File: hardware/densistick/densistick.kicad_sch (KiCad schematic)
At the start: 58 parts, among them J1 Cable, SW1 SW_Push, U1 TSL2522, U2 USBLC6-2SC6, U3 MIC4812, U4 FT260Q, U5 MIC5365-1.8YC5, U6 CAT24C08, U7 MCP4017-104E/LT

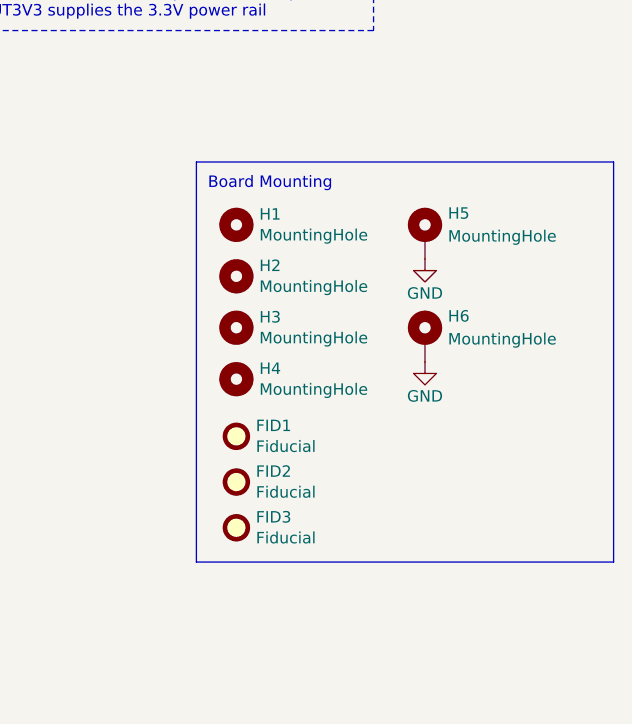
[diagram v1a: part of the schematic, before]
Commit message: Update DensiStick fiducial and position data
Add a fourth fiducial
Adjust some component silkscreen locations for more fiducial clearance
Tweak fiducial locations
Update metadata for position file exclusion
Update board date, but not revision
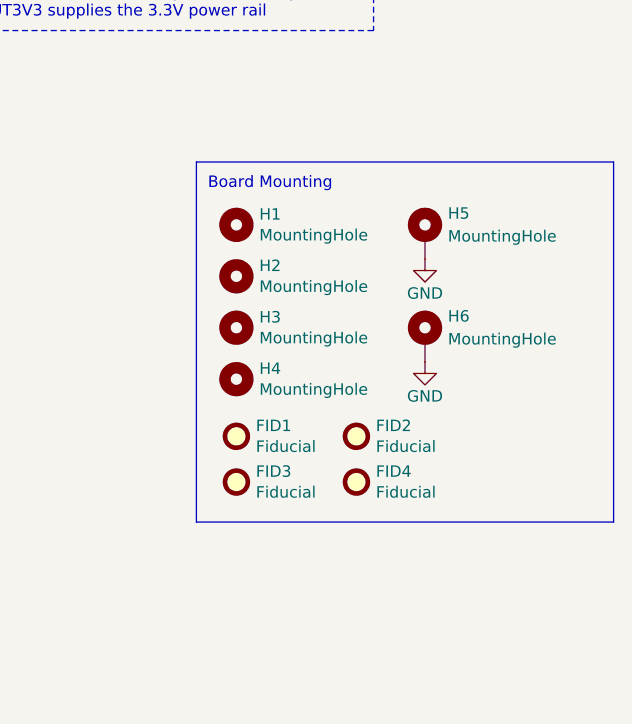
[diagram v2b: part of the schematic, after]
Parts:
- added FID4: Fiducial, Fiducial:Fiducial_1mm_Mask2mm, symbol Mechanical:Fiducial
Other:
- moved on the sheet: FID2, FID3
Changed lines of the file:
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@@
 	(title_block
 		(title "Printalyzer DensiStick")
-		(date "2025-04-30")
+		(date "2026-05-28")
 		(rev "C")
 		(company "Dektronics, Inc.")
@@
 	(rectangle
 		(start 219.075 125.73)
-		(end 265.43 170.18)
+		(end 265.43 165.735)
 		(stroke
 			(width 0)
@@
 		(in_bom no)
 		(on_board yes)
-		(in_pos_files yes)
+		(in_pos_files no)
 		(dnp no)
 		(property "Reference" "H1"
@@
 		(in_bom no)
 		(on_board yes)
-		(in_pos_files yes)
+		(in_pos_files no)
 		(dnp no)
 		(property "Reference" "H2"
@@
 		(in_bom no)
 		(on_board yes)
-		(in_pos_files yes)
+		(in_pos_files no)
 		(dnp no)
 		(property "Reference" "H3"
@@
 		(in_bom no)
 		(on_board yes)
-		(in_pos_files yes)
+		(in_pos_files no)
 		(dnp no)
 		(property "Reference" "H4"
@@
 		(in_bom no)
 		(on_board yes)
-		(in_pos_files yes)
+		(in_pos_files no)
 		(dnp no)
 		(property "Reference" "H5"
@@
 		(in_bom no)
 		(on_board yes)
-		(in_pos_files yes)
+		(in_pos_files no)
 		(dnp no)
 		(property "Reference" "H6"
@@
 	(symbol
 		(lib_id "Mechanical:Fiducial")
-		(at 223.52 161.29 0)
+		(at 236.855 156.21 0)
 		(unit 1)
 		(body_style 1)
@@
 		(dnp no)
 		(property "Reference" "FID2"
-			(at 225.679 160.1216 0)
+			(at 239.014 155.0416 0)
 			(show_name no)
 			(do_not_autoplace no)
@@
 		)
 		(property "Value" "Fiducial"
-			(at 225.679 162.433 0)
+			(at 239.014 157.353 0)
 			(show_name no)
 			(do_not_autoplace no)
@@
 		)
 		(property "Footprint" "Fiducial:Fiducial_1mm_Mask2mm"
-			(at 223.52 161.29 0)
+			(at 236.855 156.21 0)
 			(hide yes)
 			(show_name no)
@@
 		)
 		(property "Datasheet" ""
-			(at 223.52 161.29 0)
+			(at 236.855 156.21 0)
 			(hide yes)
 			(show_name no)
@@
 		)
 		(property "Description" ""
-			(at 223.52 161.29 0)
+			(at 236.855 156.21 0)
 			(hide yes)
 			(show_name no)
@@
 	(symbol
 		(lib_id "Mechanical:Fiducial")
-		(at 223.52 166.37 0)
+		(at 223.52 161.29 0)
 		(unit 1)
 		(body_style 1)
@@
 		(dnp no)
 		(property "Reference" "FID3"
-			(at 225.679 165.2016 0)
+			(at 225.679 160.1216 0)
 			(show_name no)
 			(do_not_autoplace no)
@@
 		)
 		(property "Value" "Fiducial"
-			(at 225.679 167.513 0)
+			(at 225.679 162.433 0)
 			(show_name no)
 			(do_not_autoplace no)
@@
 		)
 		(property "Footprint" "Fiducial:Fiducial_1mm_Mask2mm"
-			(at 223.52 166.37 0)
+			(at 223.52 161.29 0)
 			(hide yes)
 			(show_name no)
@@
 		)
 		(property "Datasheet" ""
-			(at 223.52 166.37 0)
+			(at 223.52 161.29 0)
 			(hide yes)
 			(show_name no)
@@
 		)
 		(property "Description" ""
-			(at 223.52 166.37 0)
+			(at 223.52 161.29 0)
 			(hide yes)
 			(show_name no)
@@
 		(in_bom no)
 		(on_board yes)
-		(in_pos_files yes)
+		(in_pos_files no)
 		(dnp no)
 		(property "Reference" "NT1"
@@
 					(unit 1)
 				)
+			)
+		)
+	)
+	(symbol
+		(lib_id "Mechanical:Fiducial")
+		(at 236.855 161.29 0)
+		(unit 1)
+		(body_style 1)
+		(exclude_from_sim no)
+		(in_bom no)
+		(on_board yes)
+		(in_pos_files yes)
+		(dnp no)
+		(property "Reference" "FID4"
+			(at 239.014 160.1216 0)
+			(show_name no)
+			(do_not_autoplace no)
+			(effects
+				(font
+					(size 1.27 1.27)
+				)
+				(justify left)
+			)
+		)
+		(property "Value" "Fiducial"
+			(at 239.014 162.433 0)
+			(show_name no)
+			(do_not_autoplace no)
+			(effects
+				(font
+					(size 1.27 1.27)
+				)
+				(justify left)
+			)
+		)
+		(property "Footprint" "Fiducial:Fiducial_1mm_Mask2mm"
+			(at 236.855 161.29 0)
+			(hide yes)
+			(show_name no)
+			(do_not_autoplace no)
+			(effects
+				(font
+					(size 1.27 1.27)
+				)
+			)
+		)
+		(property "Datasheet" ""
+			(at 236.855 161.29 0)
+			(hide yes)
+			(show_name no)
+			(do_not_autoplace no)
+			(effects
+				(font
+					(size 1.27 1.27)
+				)
+			)
+		)
+		(property "Description" ""
+			(at 236.855 161.29 0)
+			(hide yes)
+			(show_name no)
+			(do_not_autoplace no)
+			(effects
+				(font
+					(size 1.27 1.27)
+				)
+			)
+		)
+		(instances
+			(project "densistick"
+				(path "/8d0c1d66-35ef-4a53-a28f-436a11b54f42"
+					(reference "FID4")
+					(unit 1)
+				)
